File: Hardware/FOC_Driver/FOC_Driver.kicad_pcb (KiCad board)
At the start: 2 copper layers, 60 x 53 mm, 94 parts, among them IC1 DRV8323RHRGZR, J1 USB_C_Receptacle_USB2.0_16P, J3 Motor phase wire pads (solder), J5 Conn_ARM_SWD_TagConnect_TC203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, Q4 CSD18540Q5B, Q5 CSD18540Q5B, Q6 CSD18540Q5B, Q7 CSD18540Q5B, Q8 CSD18540Q5B, Q9 CSD18540Q5B, U1 STM32G431CBUx, U2 USBLC6-2SC6, U3 AP2112K-3.3, U4 MA730, U5 MR30PW, U6 XT30PW, Y1 12Mhz

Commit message: Add DNP spare pads for R9, R10, R12 (0603)
- Gate driver: R9, R10, R12 get eResistor:0603 footprint, kept DNP
- PCB: spare 0603 pads placed, excluded from BOM and assembly
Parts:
- added R10: R, eResistor:0603, F.Cu at (189.5, 91.0)
- added R12: R, eResistor:0603, F.Cu at (189.5, 93.4)
- added R9: R, eResistor:0603, F.Cu at (189.5, 88.5)

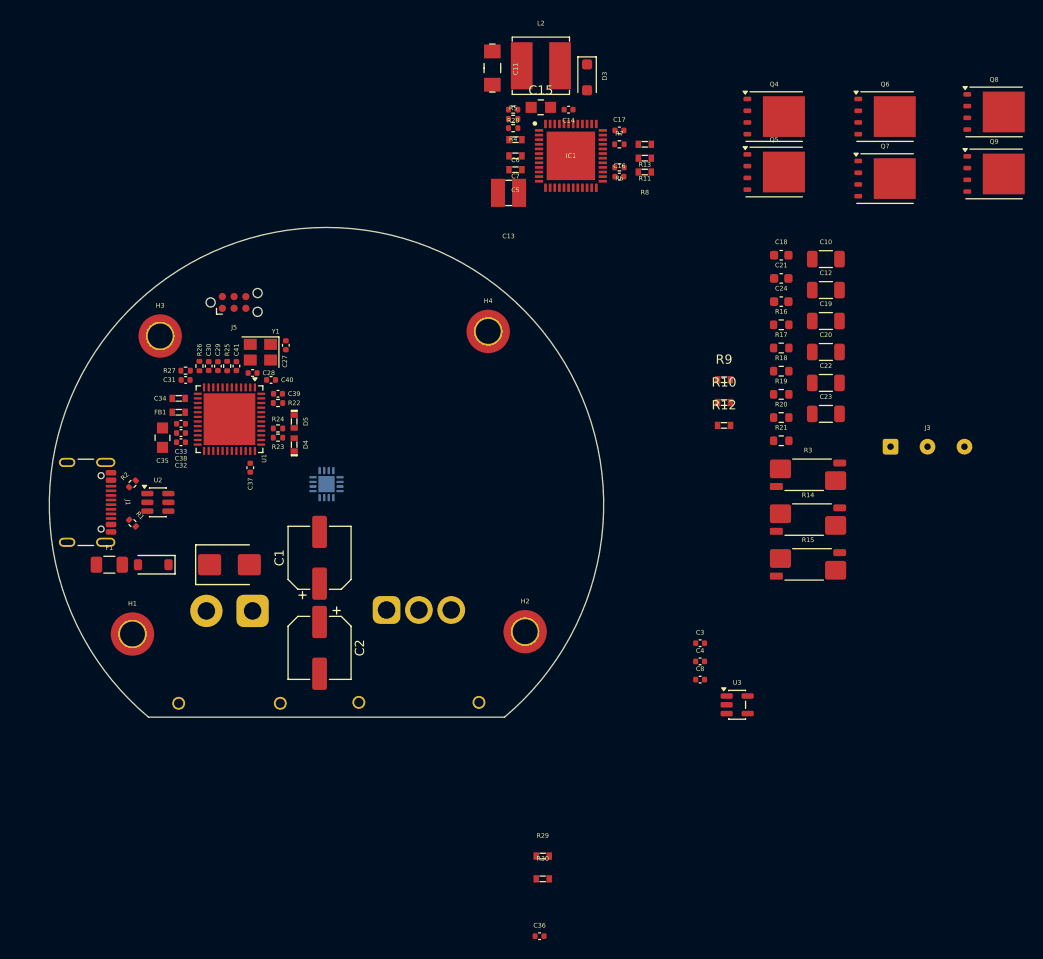
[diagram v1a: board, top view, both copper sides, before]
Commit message: Finished positioning and started layout v2
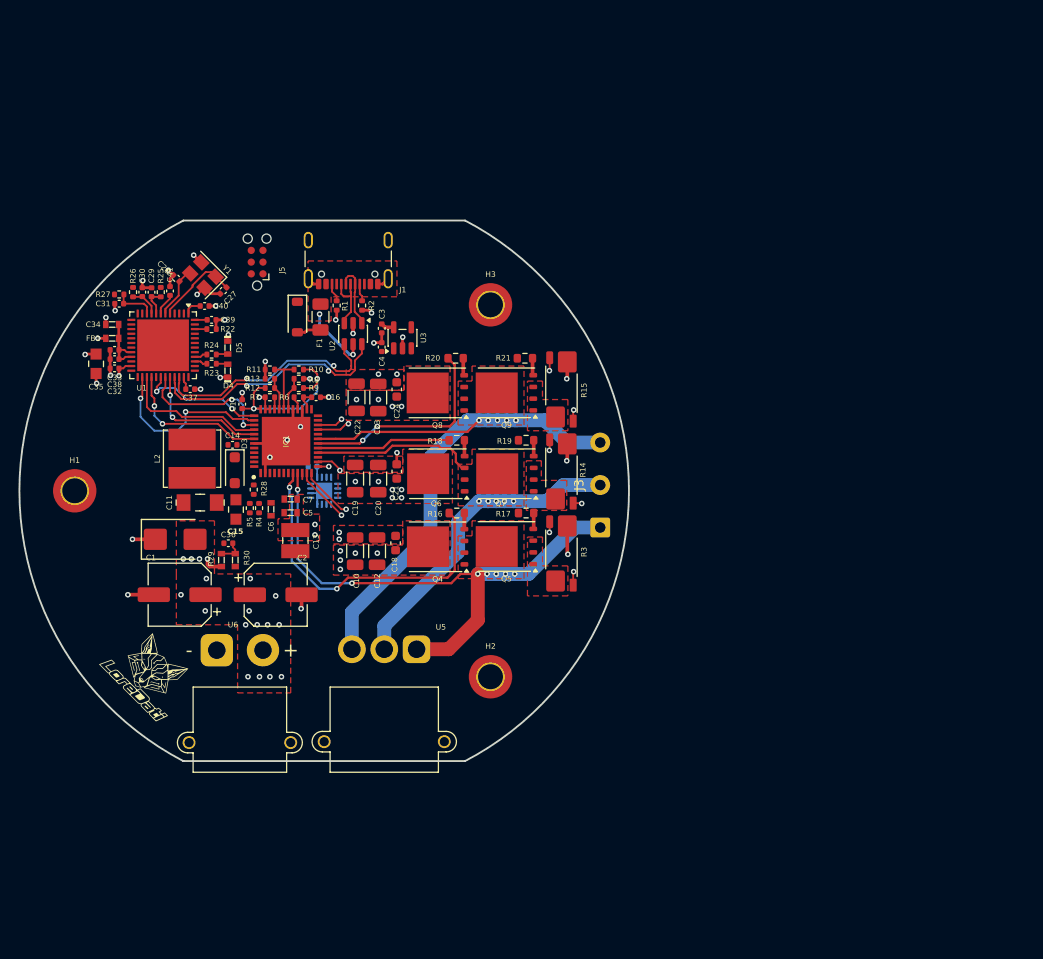
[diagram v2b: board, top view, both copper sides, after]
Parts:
- removed H4: MountingHole, MountingHole:MountingHole_2.7mm_M2.5_DIN965_Pad_TopOnly
- C8: moved to B.Cu
- J3: footprint Connector_Wire:SolderWire-0.15sqmm_1x03_P4mm_D0.5mm_OD1.5mm -> Connector_Wire:SolderWire-0.5sqmm_1x03_P4.6mm_D0.9mm_OD2.1mm
- R10, R11, R12, R13, R8, R9: footprint eResistor:0603 -> eResistor:0402
- R14, R15, R3: footprint Resistor_SMD:R_Shunt_Vishay_WSK2512_6332Metric_T1.19mm -> eResistor:R_Shunt_Vishay_WSK2512_6332Metric_T1.19mm
- U5, U6: moved to F.Cu
- moved Q8 67.5 mm to (158.5, 89.9), turned to 180 degrees
- moved Q6 61.9 mm to (158.6, 98.7), turned to 180 degrees
- moved C10 60.0 mm to (149.6, 107.0), turned to 90 degrees
- moved Q4 59.1 mm to (158.5, 106.6), turned to 180 degrees
- moved Q9 57.8 mm to (166.0, 89.9), turned to 180 degrees
- moved D3 57.1 mm to (136.6, 98.3)
- moved L2 56.9 mm to (131.9, 97.0), turned to 90 degrees
- moved C11 56.7 mm to (132.8, 101.8), turned to 0 degrees
- moved C12 56.2 mm to (152.0, 107.0), turned to 90 degrees
- moved C15 54.6 mm to (136.7, 102.5), turned to 90 degrees
- moved C36 54.2 mm to (135.9, 106.2)
- moved U3 53.8 mm to (154.7, 83.9), turned to 90 degrees
- moved C19 53.7 mm to (149.6, 99.2), turned to 90 degrees
- moved C18 52.1 mm to (154.0, 106.2), turned to 90 degrees
- moved Q7 51.9 mm to (166.0, 98.7), turned to 180 degrees
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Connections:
- R28 pad 2: +3V3 -> /Gate_Driver/VBAT(+)
- U6 pad 1: /Gate_Driver/VBAT(+) -> GND
- U6 pad 2: GND -> /Gate_Driver/VBAT(+)
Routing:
- net GND: track 0.00 -> 68.4 mm, vias 0 -> 37
- net /SHC: track 0.00 -> 63.6 mm, vias 0 -> 5
- net /SHA: track 0.00 -> 59.4 mm, vias 0 -> 7
- net /SHB: track 0.00 -> 51.8 mm, vias 0 -> 5
- net /Gate_Driver/GHA: track 0.00 -> 36.0 mm, vias 0 -> 2
- net /Gate_Driver/SPA: track 0.00 -> 35.3 mm, vias 0 -> 2
- net /Gate_Driver/SPB: track 0.00 -> 31.6 mm, vias 0 -> 2
- net /Gate_Driver/SNC: track 0.00 -> 30.5 mm, vias 0 -> 2
- net /Gate_Driver/SPC: track 0.00 -> 30.5 mm, vias 0 -> 2
- net /Gate_Driver/SNA: track 0.00 -> 30.0 mm, vias 0 -> 2
- net /Connectors/USB_D-: track 0.00 -> 27.2 mm, vias 0 -> 2
- net /Gate_Driver/SNB: track 0.00 -> 26.9 mm, vias 0 -> 2
- net /Connectors/USB_D+: track 0.00 -> 25.8 mm, vias 0 -> 2
- net /Gate_Driver/GHC: track 0.00 -> 23.2 mm, vias 0 -> 2
- net /Gate_Driver/INLA: track 0.00 -> 19.2 mm, vias 0 -> 2
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- added copper zone on In2.Cu, net +3V3
- added copper zone on F.Cu, net /Gate_Driver/VBAT(+)
- added copper zone on F.Cu, net /SHA
- added copper zone on F.Cu, net /SHB
- added copper zone on F.Cu, net /SHC
- added copper zone on F.Cu, net GND
- added copper zone on In1.Cu, net GND
- added copper zone on F.Cu, net Net-(Q5-S-Pad1)
- added copper zone on F.Cu, net Net-(Q7-S-Pad1)
- added copper zone on F.Cu, net Net-(Q9-S-Pad1)
- added copper zone on F.Cu, net VBUS
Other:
- board size 60 x 53 mm -> 66 x 58.5 mm
- copper layers 2 -> 4
- board text added: "Holes on this circumference r=27mm"
- board text added: "Motor circumference r = 31.5mm"
- board text added: "PCB circumference r = 33mm Cut at 29.250 each side"

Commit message: Layout completed
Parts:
- moved C36 27.2 mm to (123.6, 81.9), turned to 90 degrees
- moved R30 25.0 mm to (119.2, 90.0), turned to 0 degrees
- moved R29 22.9 mm to (119.2, 91.5), turned to 180 degrees
- moved D4 13.6 mm to (136.2, 73.9), turned to -90 degrees
- moved R23 12.7 mm to (135.0, 74.1), turned to -90 degrees
- moved R24 11.8 mm to (132.1, 74.1), turned to -90 degrees
- moved D5 11.4 mm to (133.4, 73.9)
- moved C28 2.30 mm to (131.7, 79.3)
- moved C27 1.74 mm to (136.1, 80.4)
- moved FB1 1.73 mm to (122.0, 85.1)
- moved C34 1.73 mm to (122.0, 83.6)
- moved R27 1.64 mm to (125.2, 80.4)
- moved C37 1.60 mm to (133.0, 90.5)
- moved Y1 1.58 mm to (134.1, 78.4)
- moved C31 1.48 mm to (125.2, 79.4)
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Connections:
- U1 pad 26: /Gate_Driver/INLA -> /Gate_Driver/INLC
- U1 pad 28: /Gate_Driver/INLC -> /Gate_Driver/INLA
- U1 pad 30: /Gate_Driver/INHA -> /Gate_Driver/INHC
- U1 pad 32: /Gate_Driver/INHC -> /Gate_Driver/INHA
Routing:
- net /Gate_Driver/VBAT(+): track 2.28 -> 45.0 mm, vias 35 -> 41
- net /LDO + Encoder/ENC_MISO: track 0.00 -> 42.4 mm, vias 0 -> 1
- net GND: track 68.4 -> 109.1 mm, vias 37 -> 50
- net /Gate_Driver/ISENSE_C: track 0.00 -> 40.1 mm, vias 0 -> 2
- net /LDO + Encoder/ENC_MOSI: track 0.00 -> 39.3 mm, vias 0 -> 1
- net /LDO + Encoder/ENC_CS: track 0.00 -> 38.0 mm, vias 0 -> 1
- net /LDO + Encoder/ENC_SCK: track 0.00 -> 36.5 mm, vias 0 -> 1
- net /Gate_Driver/ISENSE_B: track 0.00 -> 34.6 mm, vias 0 -> 2
- net +3V3: track 13.9 -> 46.8 mm, vias 3 -> 10
- net /Gate_Driver/ISENSE_A: track 0.00 -> 29.0 mm, vias 0 -> 2
- net /Gate_Driver/GLA: track 0.67 -> 28.4 mm
- net /Gate_Driver/GLC: track 0.00 -> 25.0 mm, vias 0 -> 2
- net /Gate_Driver/GLB: track 0.00 -> 22.5 mm, vias 0 -> 2
- net /Gate_Driver/NFAULT: track 1.46 -> 22.6 mm, vias 0 -> 4
- net /Connectors/NRST: track 2.37 -> 22.9 mm, vias 0 -> 2
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- added copper zone on F.Cu, net +5V
- added copper zone on In2.Cu, net +5V
- added copper zone on In2.Cu, net /Gate_Driver/VBAT(+)
